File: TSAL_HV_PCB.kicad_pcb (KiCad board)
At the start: 2 copper layers, 100 x 40 mm, 46 parts, among them J3 Conn_01x03_Socket, J4 Conn_01x03_Socket, K1 SPU01M-5, Q2 2N7002, Q3 2N7002, U1 LM393, U2 4N35, U3 TPS7B88-Q1

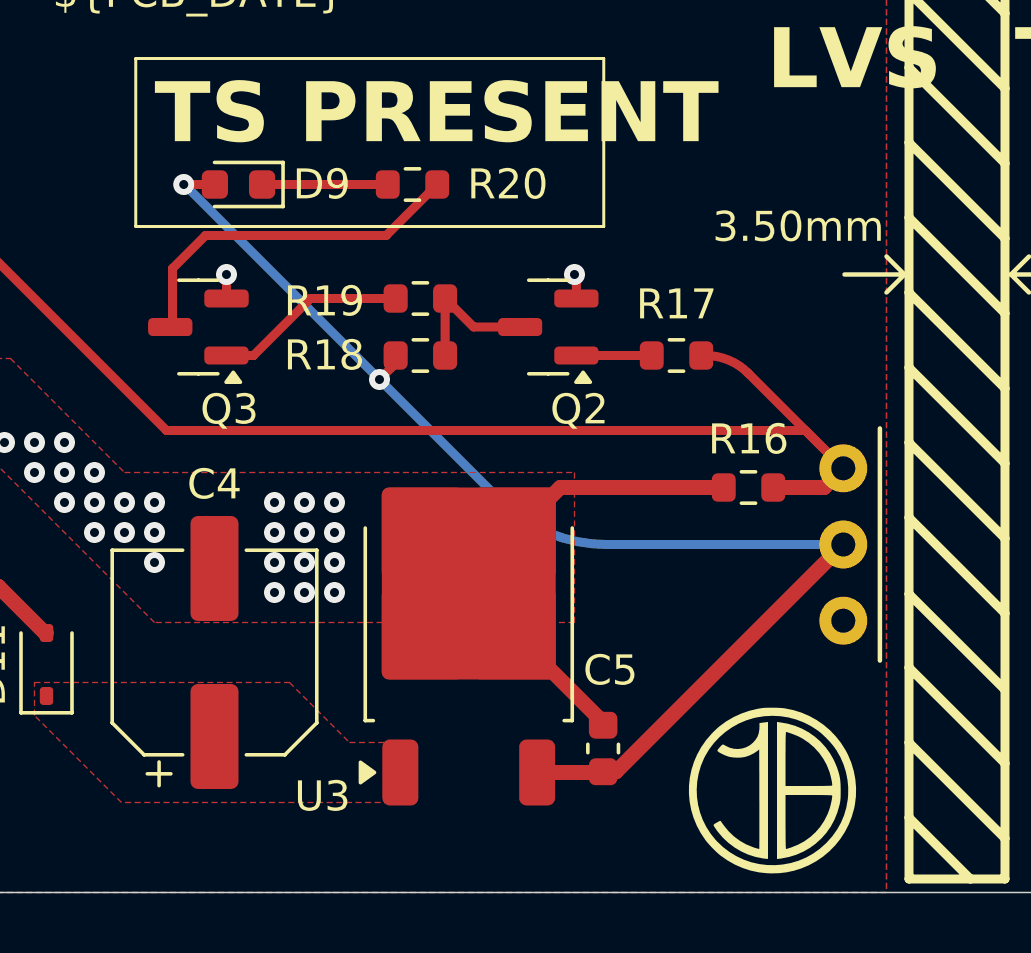
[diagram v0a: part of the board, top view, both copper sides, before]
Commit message: *: Add series resistor and pull-down to optocoupler BJT
The series resistor protects against shorts on the output and the base
pull-down helps with noise immunity.
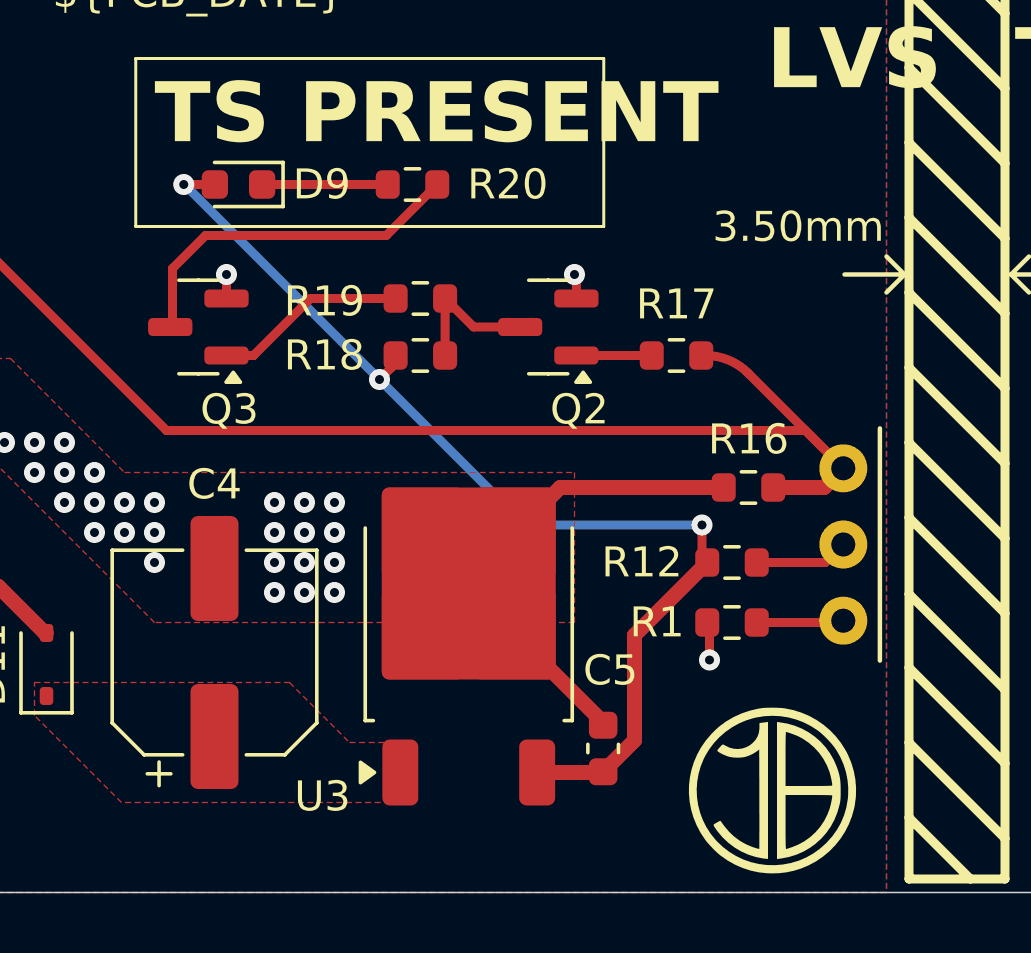
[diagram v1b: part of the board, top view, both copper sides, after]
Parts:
- added R1: 220k, Resistor_SMD:R_0603_1608Metric, F.Cu at (166.2, 86.0)
- added R12: 1k, Resistor_SMD:R_0603_1608Metric, F.Cu at (166.2, 84.0)
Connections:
- U2 pad 5: +5V -> Net-(R12-Pad2)
- U2 pad 6: unconnected-(U2-Pad6) -> Net-(R1-Pad1)
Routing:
- net +5V: track 42.1 -> 36.1 mm, vias 2 -> 3
- net Net-(R12-Pad2): track 0.00 -> 3.13 mm
- net Net-(R1-Pad1): track 0.00 -> 2.91 mm
- net GND: track 17.8 -> 19.1 mm, vias 29 -> 30
